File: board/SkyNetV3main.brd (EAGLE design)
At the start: 47.4 x 67 mm, 66 parts, among them IC1 HC_05, IC2 RF4463PRO, IC3 LPC1769, IC4 BCX17, IC5 TPS63001, IC6 MCP73871-2CCI/ML, Q1 32.768KHz, Q2 12MHz, Q3 IRLM6402, Q4 BSS138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

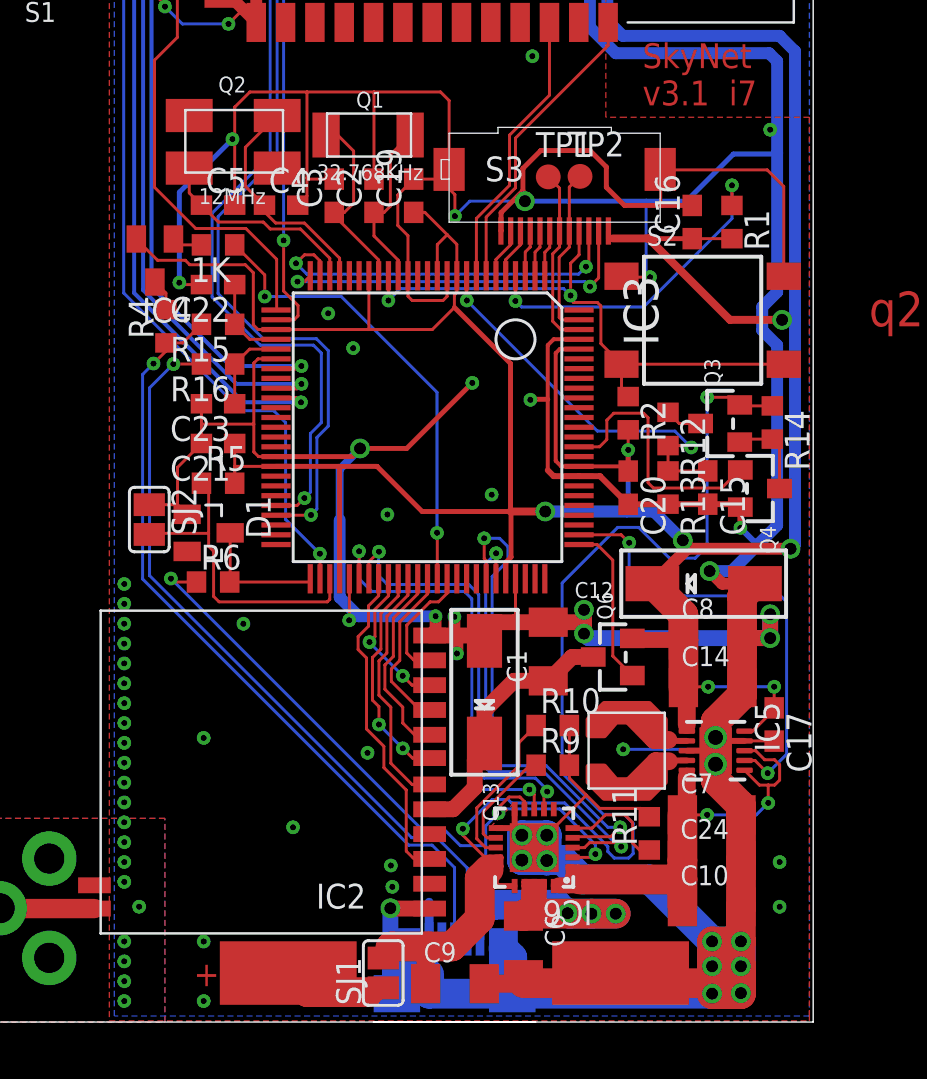
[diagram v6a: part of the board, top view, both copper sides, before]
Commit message: battery polarity revised
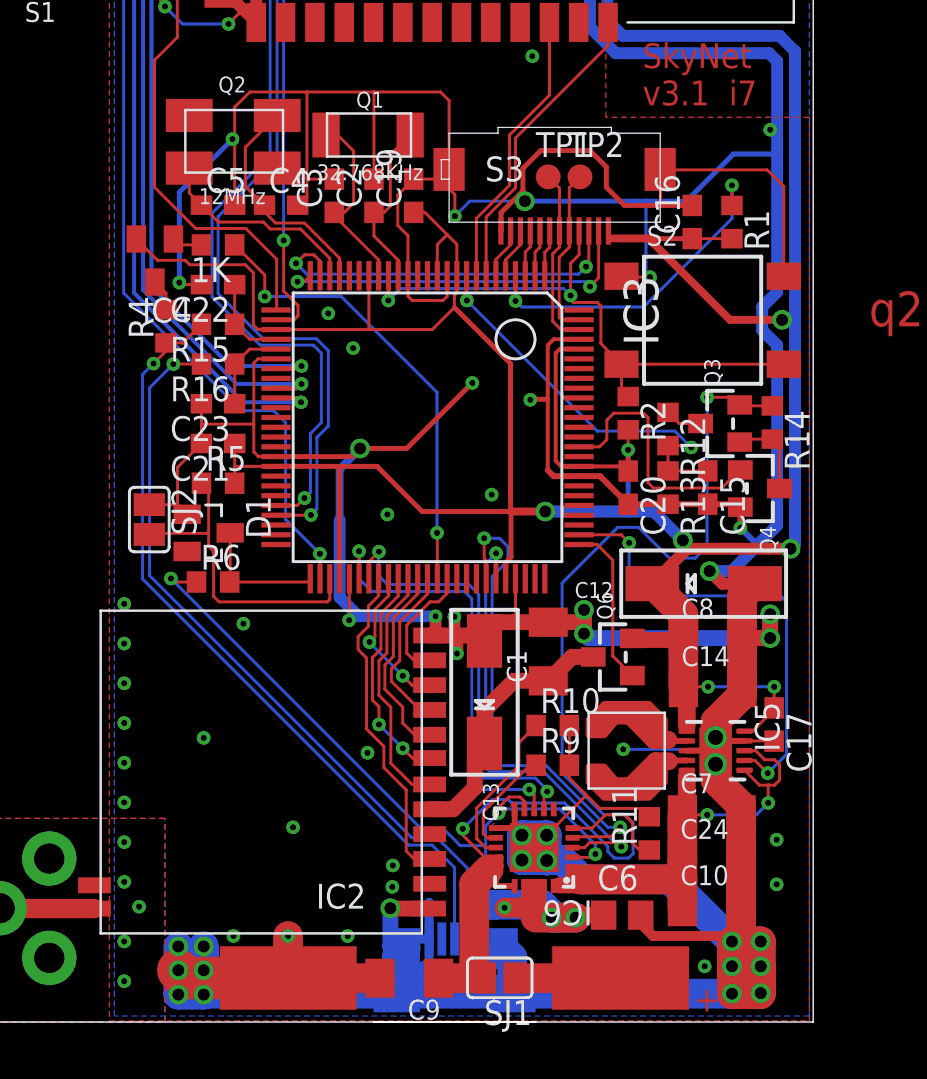
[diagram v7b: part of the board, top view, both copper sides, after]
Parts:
- C6: device rcl:C1206K -> rcl:C0805
- moved SJ1 5.97 mm to (33.9, 3.22), turned to 180 degrees
- moved C6 5.29 mm to (40.2, 6.43), turned to 0 degrees
- moved C9 2.35 mm to (29.3, 3.20), turned to 180 degrees
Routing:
- net GND: track 452.2 -> 481.2 mm, vias 75 -> 73
- net V+: track 64.7 -> 61.4 mm
- net +5V: track 57.1 -> 56.1 mm

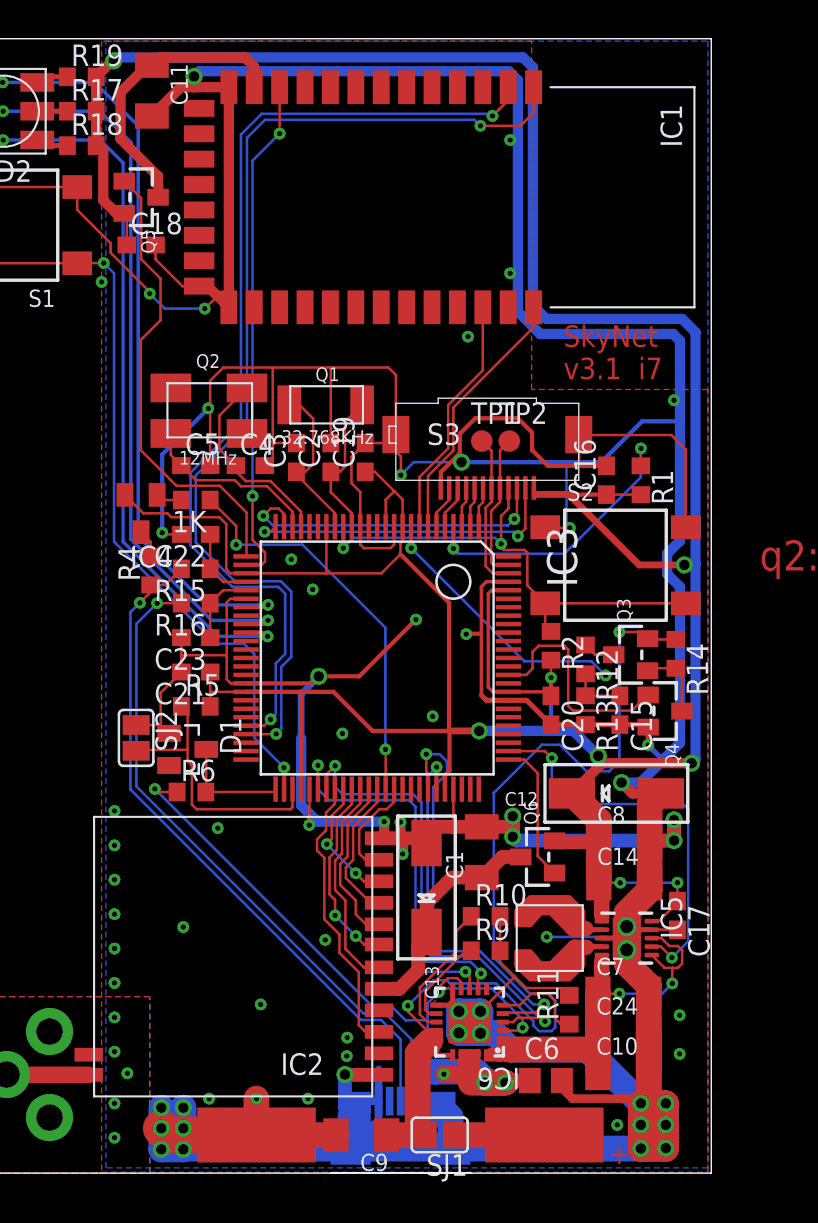
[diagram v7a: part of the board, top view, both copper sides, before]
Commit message: new connector
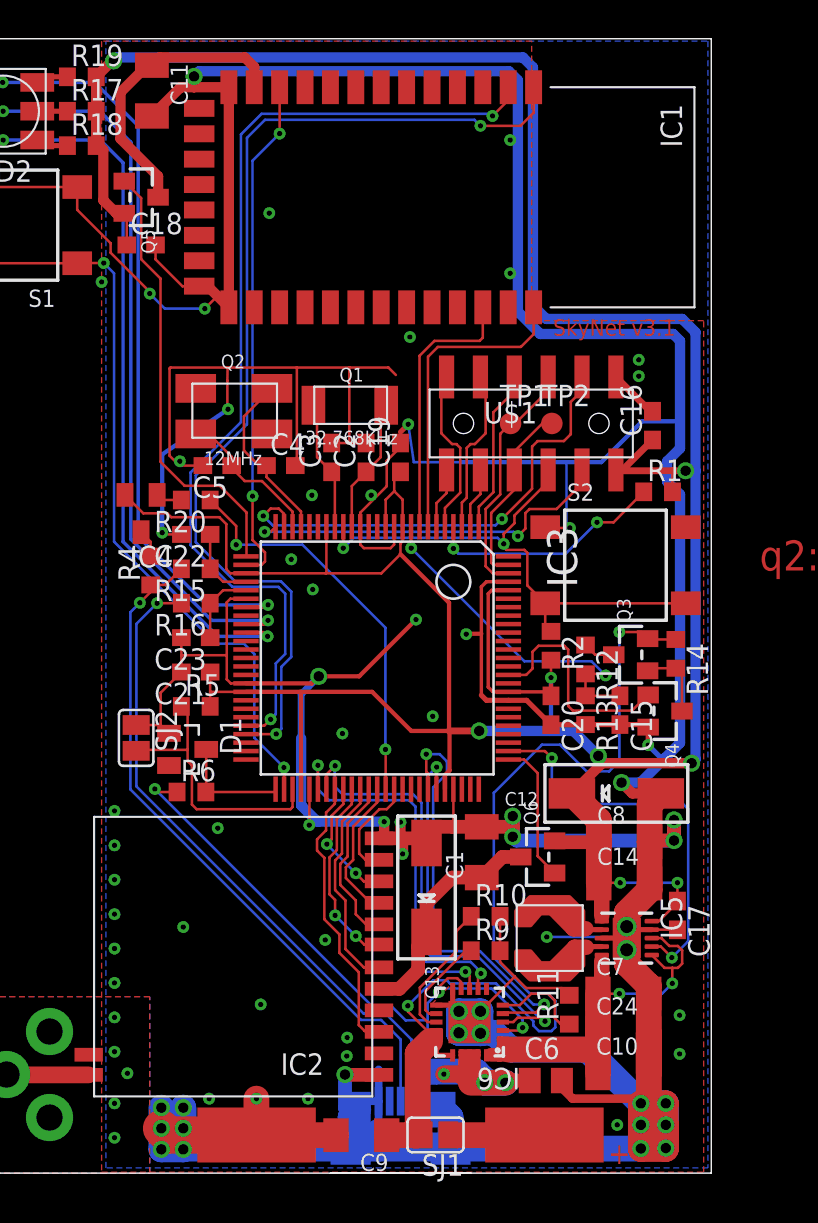
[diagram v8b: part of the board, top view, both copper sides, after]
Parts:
- removed S3: (no value), sid:MOLEX-52892-1233
- added U$1: 2X6SMD2.0, i7:2X6SMD2.00
- moved C16 4.22 mm to (46.5, 45.1)
- moved TP2 2.72 mm to (40.6, 45.2)
- moved C19 2.08 mm to (31.6, 43.2)
- moved C2 2.08 mm to (29.6, 43.2)
- moved C3 2.08 mm to (27.6, 43.2)
- moved TP1 2.00 mm to (38.1, 45.2)
- moved C4 1.80 mm to (24.6, 42.7)
- moved Q2 1.47 mm to (21.8, 46.1)
- moved Q1 1.42 mm to (28.7, 46.2)
- moved C5 1.27 mm to (20.8, 42.7), turned to 180 degrees
- moved R1 1.23 mm to (46.8, 41.2), turned to 0 degrees
- moved SJ1 0.25 mm to (33.7, 3.22)
- renumbered 1K to R20
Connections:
- net +3V3: now also U$1.P$11; no longer S3.P$1
- net AD-EXT: now also U$1.P$1; no longer S3.P$11
- net GND: now also U$1.P$12; no longer S3.P$12, S3.P$GND1, S3.P$GND2
- net JTAG_TCK: now also U$1.P$2; no longer S3.P$10
- net JTAG_TDI: now also U$1.P$3; no longer S3.P$8
- net JTAG_TDO: now also U$1.P$6; no longer S3.P$7
- net JTAG_TMS: now also U$1.P$4; no longer S3.P$9
- net RESET: now also U$1.P$7; no longer S3.P$4
- net RX: now also U$1.P$5; no longer S3.P$5
- net SCL-EXT: now also U$1.P$10; no longer S3.P$3
- net SDA-EXT: now also U$1.P$9; no longer S3.P$2
- net TX: now also U$1.P$8; no longer S3.P$6
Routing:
- net GND: track 481.2 -> 460.3 mm, vias 73 -> 77
- net +3V3: track 227.8 -> 218.0 mm
- net SCL-EXT: track 19.4 -> 28.0 mm
- net JTAG_TCK: track 2.60 -> 9.96 mm
- net JTAG_TDO: track 2.40 -> 9.72 mm
- net JTAG_TMS: track 2.40 -> 9.71 mm
- net TX: track 9.29 -> 14.4 mm
- net SDA-EXT: track 18.9 -> 22.3 mm
- net JTAG-TRST: track 17.2 -> 14.3 mm
- net BT-AT: track 15.5 -> 18.4 mm
- net RX: track 8.70 -> 11.1 mm
- net RTCX2: track 9.79 -> 7.81 mm
- net RESET: track 29.9 -> 31.8 mm
- net XTAL2: track 10.7 -> 8.93 mm
- net BT-CN: track 14.5 -> 16.1 mm
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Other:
- board text added: "SkyNet v3.1"
- board text removed: "SkyNet v3.1 i7"
